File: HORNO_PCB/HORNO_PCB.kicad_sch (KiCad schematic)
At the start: 249 parts, among them J0_1 Terminales de tornillo espaci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, J0_10 Terminales de tornillo espaci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, J0_13 Terminales de tornillo espaci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, J0_14 Terminales de tornillo espaci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, J0_16 Terminales de tornillo espaci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, J0_18 Terminales de tornillo espaci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, J0_19 Terminales de tornillo espaci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, J0_2 Terminales de tornillo espaci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, J0_20 Terminales de tornillo espaci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, J0_21 Terminales de tornillo espaci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, J0_22 Terminales de tornillo espaci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, J0_23 Terminales de tornillo espaci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, J0_24 Terminales de tornillo espaci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, J0_25 Terminales de tornillo espaci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, J0_26 Terminales de tornillo espaci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, J0_3 Terminales de tornillo espaci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, J0_5 Terminales de tornillo espaci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, J0_6 Terminales de tornillo espaci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, J0_7 Terminales de tornillo espaci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, J0_8 Terminales de tornillo espaci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, J0_9 Terminales de tornillo espaci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, J1 20 Pin 2.54mm Header Male Bre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, J2 20 Pin 2.54mm Header Male Bre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, J3 20 Pin 2.54mm Header Male Bre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, J4 20 Pin 2.54mm Header Male Bre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, K1 Fujitsu FTR-LYCA005x, K2 Fujitsu FTR-LYCA005x, K3 Fujitsu FTR-LYCA005x, K4 Fujitsu FTR-LYCA005x, Q1 2N2222, Q2 2N2222, Q3 2N2222, Q4 2N2222, Q5 BTA16-800B, Q6 IRG4PF50W, Q7 IRG4PF50W, U1 TLP521-1, U10 LM741, U11 LM741, U12 LM741, U13 MOC3021M, U14 TLP521-1, U15 TLP250, U16 TLP521-1, U17 LM741, U18 LM741, U19 TLP250, U2 TLP521-1, U20 L298HN Multiwatt15 H, U21 TLP521-1, U22 TLP521-1, U23 TLP521-1, U3 TLP521-1, U4 TLP521-1, U5 TLP521-1, U6 TLP521-1, U7 TLP521-1, U8 TLP521-1, U9 LM741

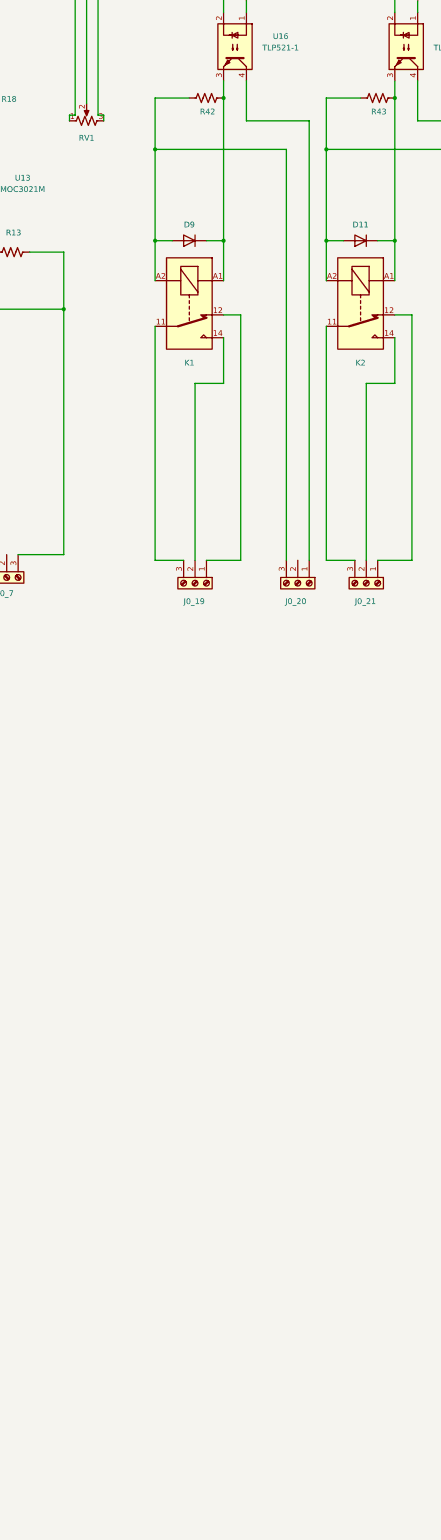
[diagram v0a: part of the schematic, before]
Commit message: Modificando salida de relé
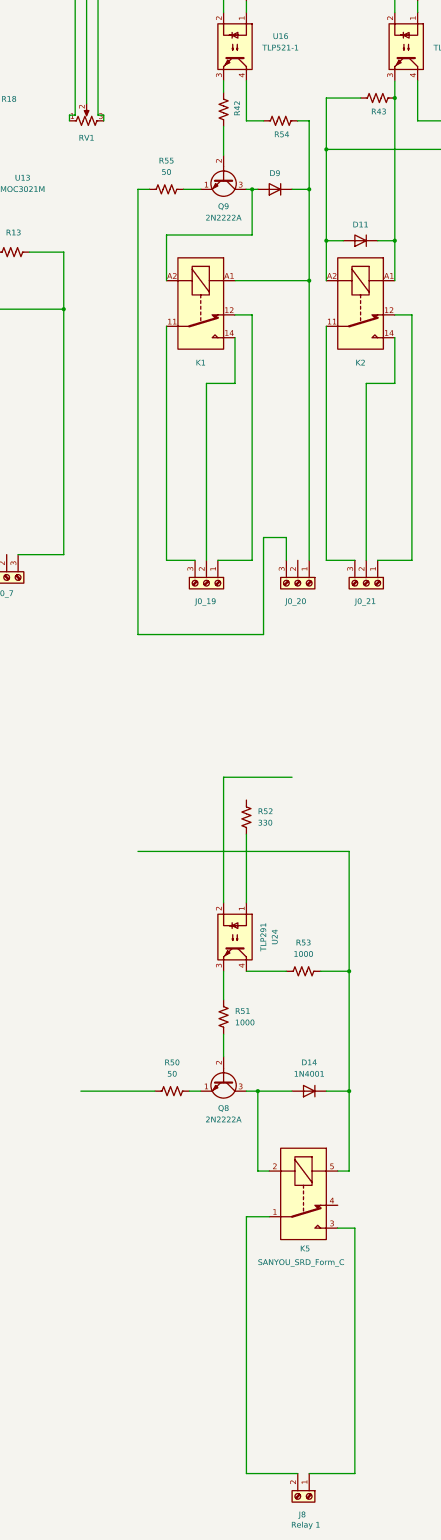
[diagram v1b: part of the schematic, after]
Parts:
- added D14: 1N4001, Diode_THT:D_DO-41_SOD81_P10.16mm_Horizontal, symbol Diode:1N4001
- added J8: Relay 1, TerminalBlock_Phoenix:TerminalBlock_Phoenix_MKDS-1,5-2-5.08_1x02_P5.08mm_Horizontal, symbol Connector:Screw_Terminal_01x02
- added K5: SANYOU_SRD_Form_C, Relay_THT:Relay_SPDT_SANYOU_SRD_Series_Form_C, symbol Relay:SANYOU_SRD_Form_C
- added Q8, Q9: 2N2222A, Package_TO_SOT_THT:TO-92, symbol Transistor_BJT:Q_NPN_EBC
- added R50, R55: 50, Resistor_THT:R_Axial_DIN0309_L9.0mm_D3.2mm_P12.70mm_Horizontal, symbol Device:R_US
- added R51, R53: 1000, Resistor_THT:R_Axial_DIN0207_L6.3mm_D2.5mm_P10.16mm_Horizontal, symbol Device:R_US
- added R52: 330, Resistor_THT:R_Axial_DIN0207_L6.3mm_D2.5mm_P10.16mm_Horizontal, symbol Device:R_US
- added R54: Depende de la tensión aplicada a la bobina del re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, Resistor_THT:R_Axial_DIN0309_L9.0mm_D3.2mm_P15.24mm_Horizontal, symbol Device:R_US
- added U24: TLP291, Package_SO:SOIC-4_4.55x2.6mm_P1.27mm, symbol Isolator:TLP291
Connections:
- net at J0_20.1 (Pin_1): now also D9.1 (K), K1.A1, R54.2; no longer U16.4
- net at D9.2 (A), K1.A2: now also Q9.3 (C); no longer J0_20.3 (Pin_3), R42.1
- net at R42.2, U16.3: no longer D9.1 (K), K1.A1
- new net: J0_20.3 (Pin_3), R55.2
- new net: J8.2 (Pin_2), K5.1
- new net: D14.2 (A), K5.2, Q8.3 (C)
- new net: J8.1 (Pin_1), K5.3
- new net: D14.1 (K), K5.5, R53.1
- new net: Q9.1 (E), R55.1
- new net: R54.1, U16.4
- new net: Q9.2 (B), R42.1
- new net: R52.2, U24.1
- new net: R51.2, U24.3
- new net: R53.2, U24.4
- new net: Q8.1 (E), R50.1
- new net: Q8.2 (B), R51.1
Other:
- moved on the sheet: D9, J0_19, K1, R42

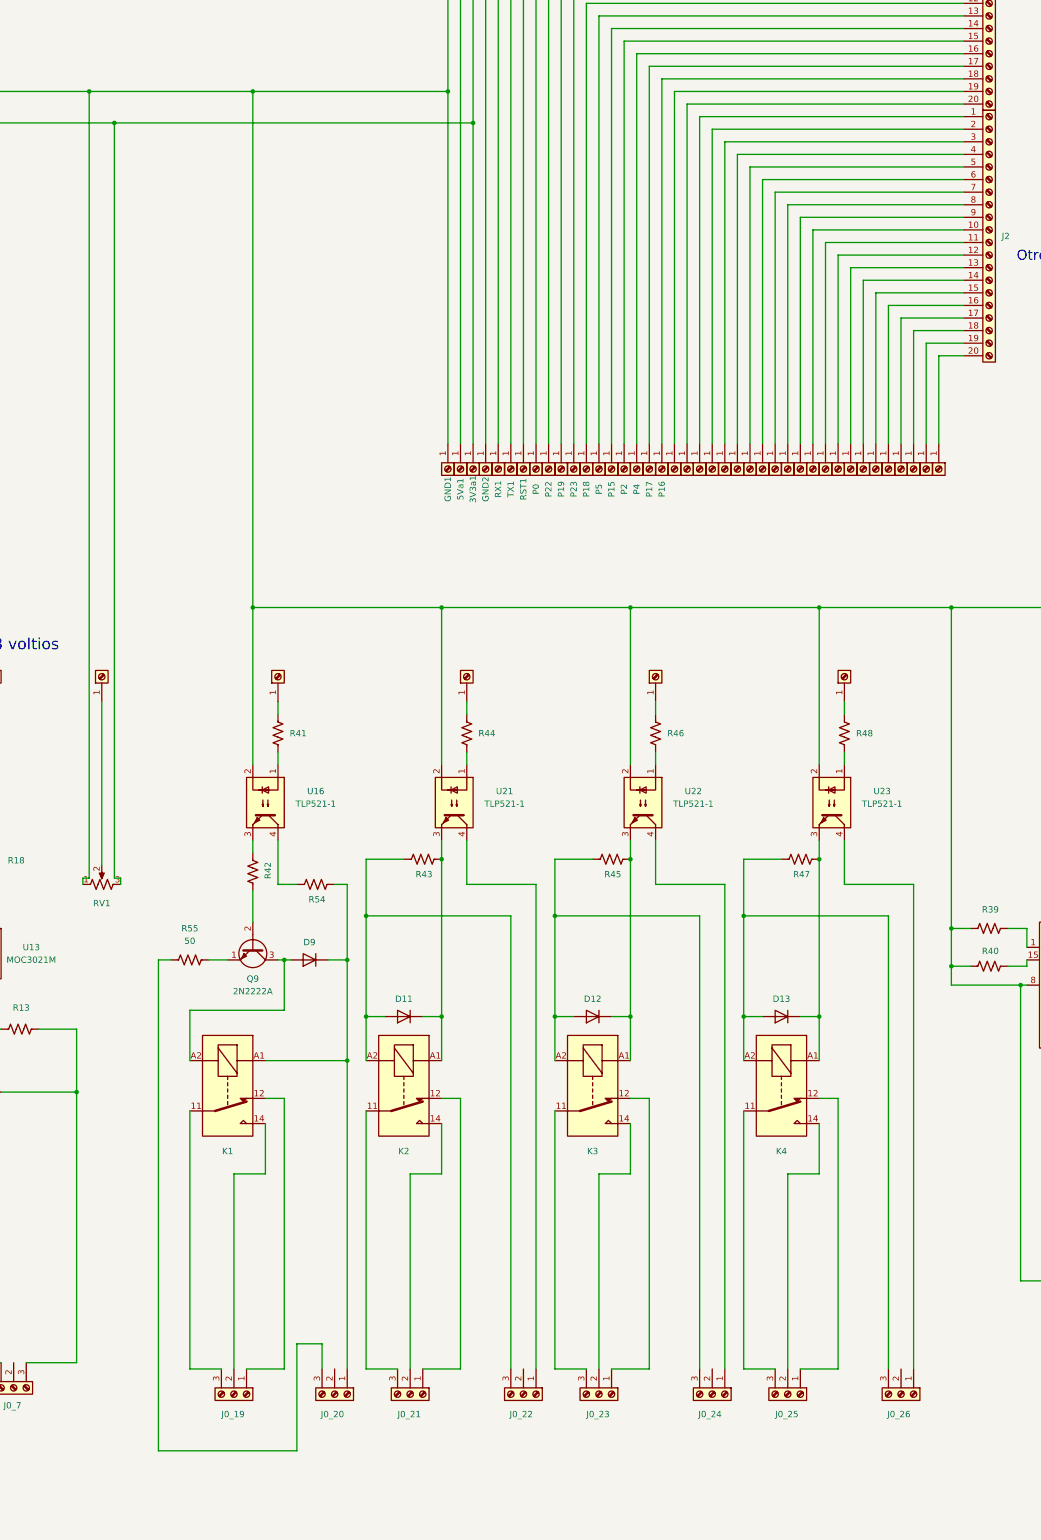
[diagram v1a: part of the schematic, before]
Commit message: Modificando salida de relé
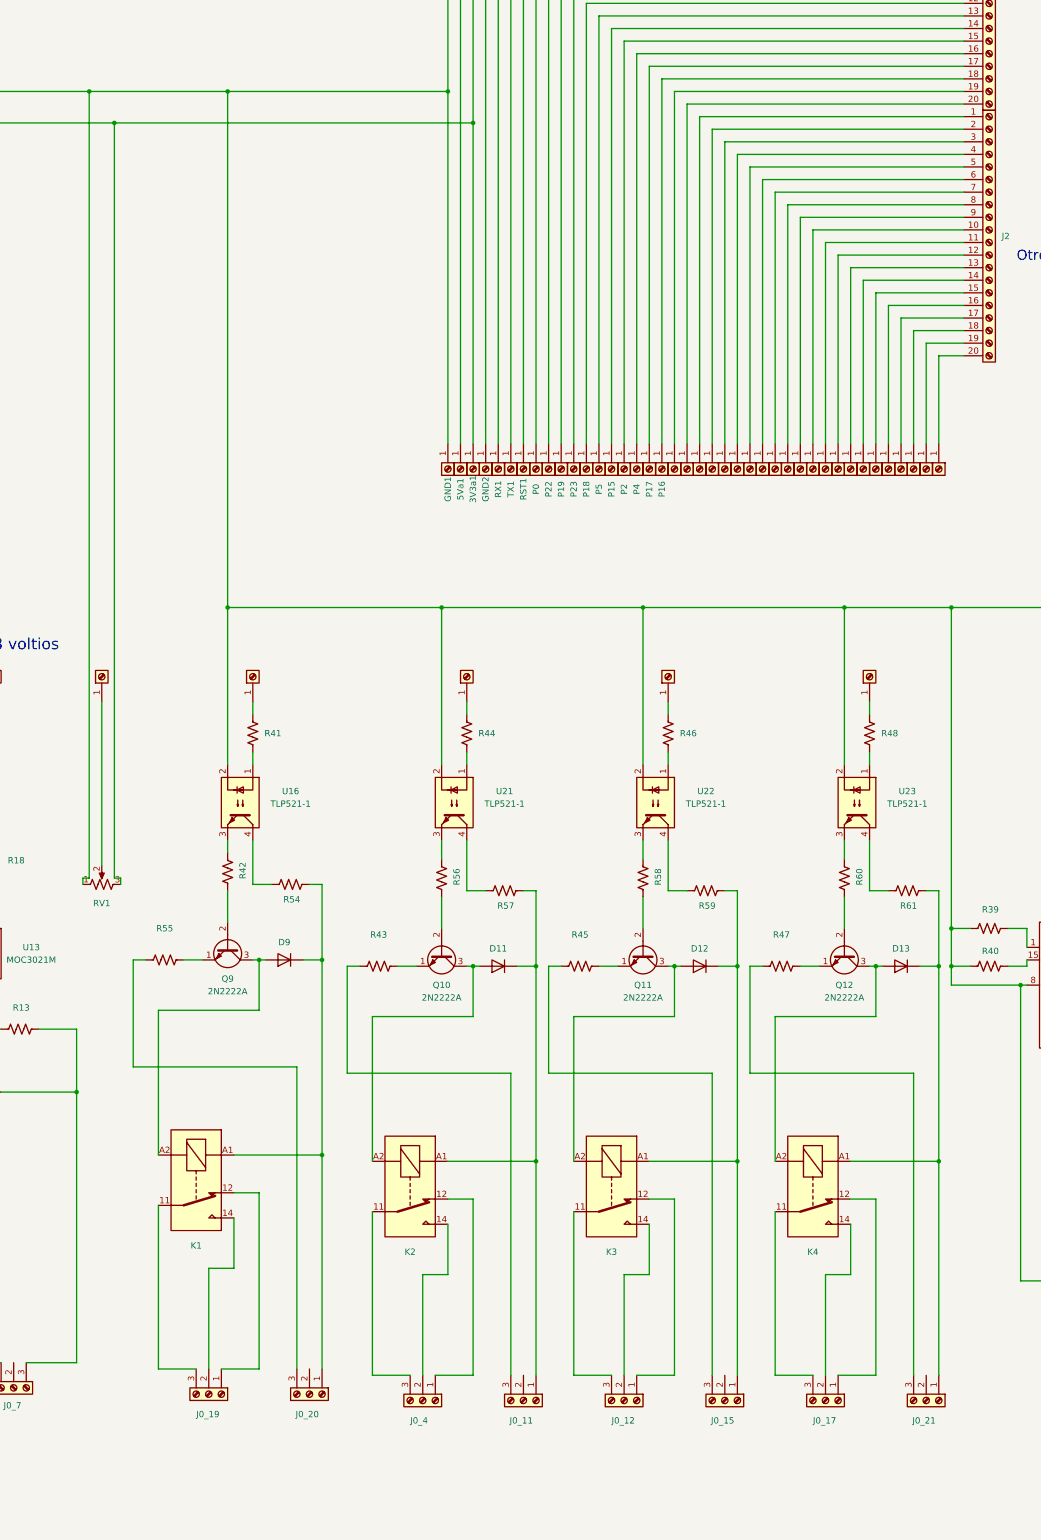
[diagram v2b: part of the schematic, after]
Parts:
- removed J0_22, J0_23, J0_24, J0_25, J0_26: Terminales de tornillo espaciados en 3.5mm, TerminalBlock_Phoenix:TerminalBlock_Phoenix_PT-1,5-3-3.5-H_1x03_P3.50mm_Horizontal, symbol Connector:Screw_Terminal_01x03
- added J0_11, J0_12, J0_15, J0_17, J0_4: Terminales de tornillo espaciados en 3.5mm, TerminalBlock_Phoenix:TerminalBlock_Phoenix_PT-1,5-3-3.5-H_1x03_P3.50mm_Horizontal, symbol Connector:Screw_Terminal_01x03
- added Q10, Q11, Q12: 2N2222A, Package_TO_SOT_THT:TO-92, symbol Transistor_BJT:Q_NPN_EBC
- added R56, R57, R58, R59, R60, R61: Depende de la tensión aplicada a la bobina del re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, Resistor_THT:R_Axial_DIN0309_L9.0mm_D3.2mm_P15.24mm_Horizontal, symbol Device:R_US
- R43, R45, R47: footprint Resistor_THT:R_Axial_DIN0309_L9.0mm_D3.2mm_P15.24mm_Horizontal -> Resistor_THT:R_Axial_DIN0309_L9.0mm_D3.2mm_P12.70mm_Horizontal
- R55: value 50 -> Depende de la tensión aplicada a la bobina del rele
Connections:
- net at D11.1 (K), K2.A1: now also J0_11.1 (Pin_1), R57.2; no longer R43.2, U21.3
- net at U21.4: now also R57.1
- net at K4.11: now also J0_17.3 (Pin_3)
- net at K4.12: now also J0_17.1 (Pin_1)
- net at K4.14: now also J0_17.2 (Pin_2)
- net at D13.1 (K), K4.A1: now also J0_21.1 (Pin_1), R61.2; no longer R47.2, U23.3
- net at D13.2 (A), K4.A2: now also Q12.3 (C); no longer R47.1
- net at D11.2 (A), K2.A2: now also Q10.3 (C); no longer R43.1
- net at K2.12: now also J0_4.1 (Pin_1); no longer J0_21.1 (Pin_1)
- net at K2.14: now also J0_4.2 (Pin_2); no longer J0_21.2 (Pin_2)
- net at K2.11: now also J0_4.3 (Pin_3); no longer J0_21.3 (Pin_3)
- net at D12.1 (K), K3.A1: now also J0_15.1 (Pin_1), R59.2; no longer R45.2, U22.3
- net at U22.4: now also R59.1
- net at K3.11: now also J0_12.3 (Pin_3)
- net at K3.12: now also J0_12.1 (Pin_1)
- net at K3.14: now also J0_12.2 (Pin_2)
- net at D12.2 (A), K3.A2: now also Q11.3 (C); no longer R45.1
- net at U23.4: now also R61.1
- new net: R56.2, U21.3
- new net: Q11.1 (E), R45.1
- new net: Q11.2 (B), R58.1
- new net: J0_11.3 (Pin_3), R43.2
- new net: Q12.2 (B), R60.1
- new net: R60.2, U23.3
- new net: R58.2, U22.3
- new net: Q10.1 (E), R43.1
- new net: Q10.2 (B), R56.1
- new net: Q12.1 (E), R47.1
- new net: J0_21.3 (Pin_3), R47.2
- new net: J0_15.3 (Pin_3), R45.2
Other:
- moved on the sheet: D9, J0_19, J0_20, K1, Q9, R41, R42, R46, R48, R54, R55, U16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
